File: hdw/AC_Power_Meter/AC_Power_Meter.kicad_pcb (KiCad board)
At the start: 2 copper layers, 100 x 100 mm, 272 parts, among them J1001 USB_B_Mini, J1701 Ext_SW_Toggle, J201 HT_IN, J202 NEUT_IN, J203 EARTH_IN, J401 HT_OUT, J402 NEUT_OUT, J403 EARTH_OUT, J501 AUX_IN, J801 Prog, Q1501 BT139-600, Q1701 2N7002, Q501 DMP3099L-7, SW1702 MRESET, SW1703 SW_Toggle, U1001 LT6700-1-S6, U1002 FT234XD, U1003 74LVC1G06, U1004 TPD3S014DBVR, U1101 ISO7321C, U1201 SSD1306, U1401 LTV-356T, U1402 74LVC1G17, U1501 74LVC1G32, U1502 FOD4218, U1601 74LVC1G06, U1602 74LVC1G06, U1603 74LVC1G06, U1604 74LVC1G06, U1605 74LVC1G06, U1606 74LVC1G06, U1607 74LVC1G06, U1701 TLC555CPS, U1702 TLC555CPS, U301 ACS722LLCTR-20AB, U501 LT6700-1-S6, U502 74LVC1G17, U601 74LVC1G17, U602 LT3973-DD, U701 PIC18LF67K40-I/PT, U801 TL331, U802 74LVC1G86, U901 LTC6240IS5, U902 LTC6240IS5, U903 LTC6240IS5, U904 LTC6240IS5, X701 ASV-16.000MHz

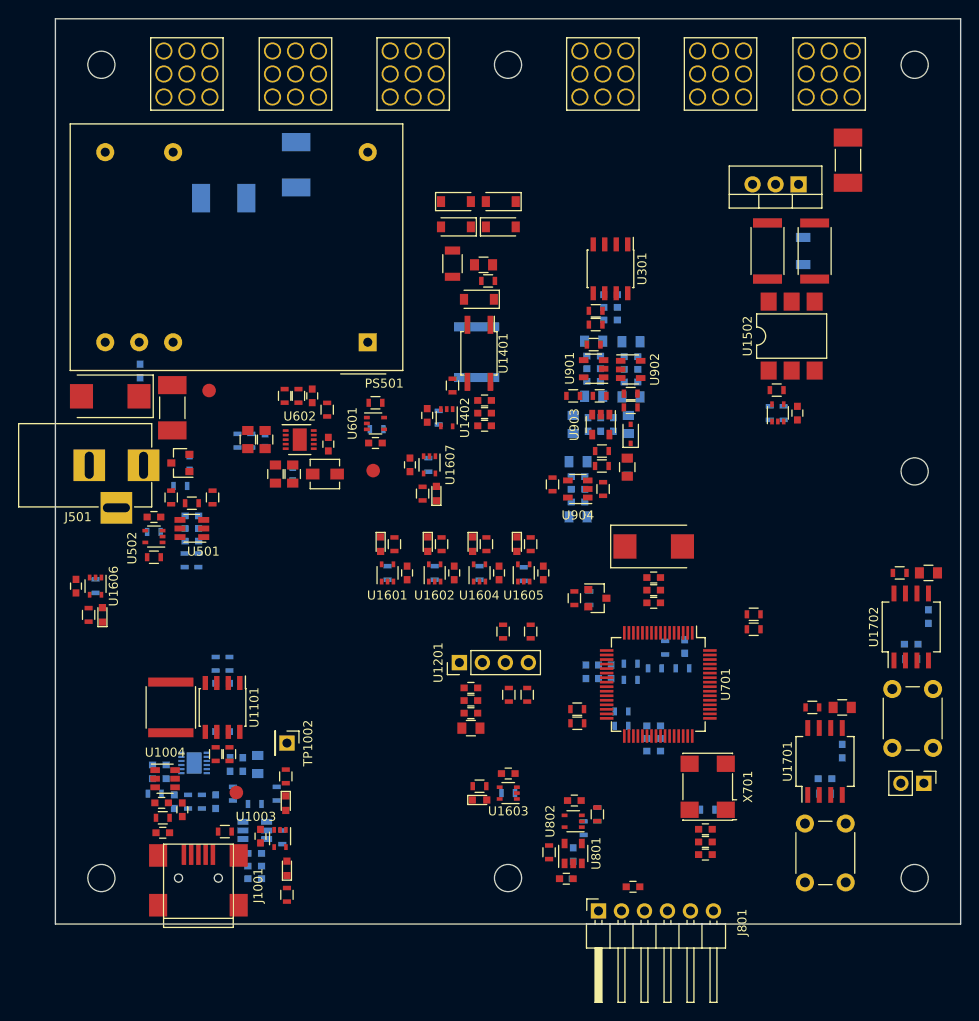
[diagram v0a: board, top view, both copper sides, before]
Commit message: Routed much more of the board, design rule fixes
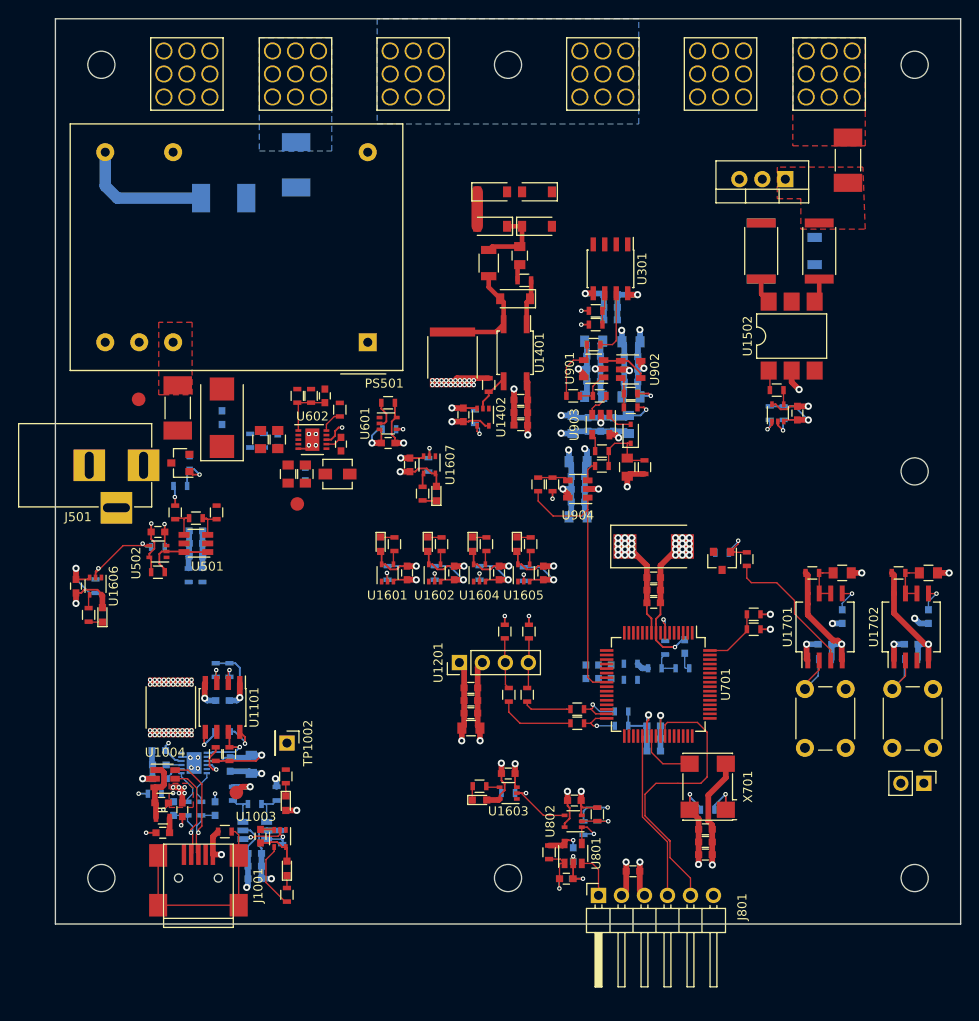
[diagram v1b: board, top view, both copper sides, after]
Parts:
- C1402, R907: moved to F.Cu
- moved R1706 19.5 mm to (148.0, 110.9)
- moved R1705 15.5 mm to (145.3, 110.2), turned to 180 degrees
- moved C1701 14.9 mm to (158.6, 117.2)
- moved C1705 14.9 mm to (158.6, 112.4)
- moved R1703 14.9 mm to (155.3, 112.4)
- moved U1701 14.9 mm to (156.7, 118.4)
- moved R1701 14.9 mm to (156.7, 121.9)
- moved SW1702 14.9 mm to (158.9, 125.2)
- moved C1703 14.9 mm to (156.7, 120.3)
- moved Q1701 14.4 mm to (145.3, 111.1), turned to 270 degrees
- moved C505 12.6 mm to (90.0, 95.2), turned to 90 degrees
- moved C504 10.4 mm to (90.0, 95.2)
- moved C1006 9.41 mm to (83.1, 132.0), turned to 180 degrees
- moved TP601 9.16 mm to (98.4, 104.8)
- moved TP501 7.84 mm to (80.8, 93.2)
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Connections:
- R1101 pad 2: GND -> +3V3
- R1102 pad 2: GND -> +3V3
- R1103 pad 2: GND_USB -> +5V_USB
- R1104 pad 2: GND_USB -> +5V_USB
- U1004 pad 5: /USB UART Bridge/CONN_USB+ -> /USB UART Bridge/CONN_USB-
- U1004 pad 6: /USB UART Bridge/CONN_USB- -> /USB UART Bridge/CONN_USB+
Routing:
- net +3V3: track 0.00 -> 214.7 mm, vias 0 -> 48
- net GND: track 0.00 -> 194.7 mm, vias 0 -> 98
- net +5V_USB: track 0.00 -> 40.4 mm, vias 0 -> 13
- net GND_USB: track 0.00 -> 33.1 mm, vias 0 -> 34
- net ICSPCLK: track 0.00 -> 32.4 mm
- net ISNS_ADC: track 0.00 -> 29.7 mm
- net Net-(J1001-Pad6): track 0.00 -> 23.1 mm
- net ICSPDAT: track 0.00 -> 18.8 mm
- net Net-(R1706-Pad2): track 0.00 -> 15.9 mm
- net /USB UART Bridge/CONN_USB+: track 0.00 -> 15.5 mm, vias 0 -> 1
- net Net-(F501-Pad1): track 0.00 -> 14.9 mm
- net /USB UART Bridge/CONN_USB-: track 0.00 -> 14.3 mm, vias 0 -> 1
- net POS12_PGOOD: track 0.00 -> 12.1 mm, vias 0 -> 2
- net GNDPWR: track 0.00 -> 12.0 mm
- net ~MCLR: track 0.00 -> 8.97 mm, vias 0 -> 1
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- added copper zone on PWR, net +3V3
- added copper zone on F.Cu, net +5V_USB
- added copper zone on PWR, net +5V_USB
- added copper zone on B.Cu, net Earth_Protective
- added copper zone on GND, net GND
- added copper zone on GND, net GND_USB
- added copper zone on B.Cu, net Net-(F201-Pad2)
- added copper zone on F.Cu, net Net-(F401-Pad1)
- added copper zone on F.Cu, net Net-(F502-Pad2)
- added copper zone on F.Cu, net TRIAC_HT_OUT
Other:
- copper layers 2 -> 4
- net class Default: trace_width 0.1016 -> 0.2032; via_dia 0.8 -> 0.5; via_drill 0.4 -> 0.25
- net class Power_HV_Tight added: clearance 0.127, trace_width 1.27, via_dia 0.8, via_drill 0.4
- net class Signal: trace_width 0.1016 -> 0.1524
- board text added: "* Add MU Logo * Label all LEDs * Label all connectors * Add layer copper labels * Add ESD warning * Add high voltage warning"

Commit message: MOAR ROUTING
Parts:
- C301, C302, C303: moved to F.Cu
- R301, R302, U301: moved to B.Cu
- moved D1404 12.3 mm to (117.1, 82.2), turned to 90 degrees
- moved D1401 12.1 mm to (113.2, 77.3), turned to 90 degrees
- moved D1403 10.6 mm to (113.2, 82.2), turned to 270 degrees
- moved D1402 10.4 mm to (117.1, 77.3), turned to 270 degrees
- moved R606 4.23 mm to (95.6, 94.4), turned to 90 degrees
- moved R301 3.88 mm to (135.1, 83.9), turned to 180 degrees
- moved R302 3.88 mm to (135.1, 82.4), turned to 180 degrees
- moved R605 3.48 mm to (94.1, 94.4), turned to 270 degrees
- moved C1403 1.59 mm to (123.7, 94.7)
- moved U1402 1.59 mm to (119.5, 96.6)
- moved C1402 1.59 mm to (116.1, 90.0)
- moved R1401 1.59 mm to (120.1, 79.6)
- moved R1402 1.59 mm to (124.1, 81.5)
- moved R1404 1.59 mm to (118.6, 96.6)
- moved C1404 1.59 mm to (123.7, 96.1)
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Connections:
- U301 pad 1: ISNS_HT_OUT -> HT
- U301 pad 2: ISNS_HT_OUT -> HT
- U301 pad 3: HT -> ISNS_HT_OUT
- U301 pad 4: HT -> ISNS_HT_OUT
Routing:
- net NEUT: track 3.81 -> 44.9 mm
- net ISNS_HT_OUT: track 0.00 -> 30.0 mm
- net HT: track 0.00 -> 26.8 mm, vias 0 -> 1
- net Net-(Q1501-Pad3): track 2.70 -> 28.7 mm
- net TRIAC_HT_OUT: track 0.00 -> 24.7 mm
- net GND: track 194.7 -> 214.8 mm, vias 98 -> 100
- net Net-(C1401-Pad2): track 7.58 -> 18.1 mm, vias 0 -> 2
- net Net-(C605-Pad2): track 0.00 -> 8.76 mm
- net Net-(C1502-Pad1): track 0.00 -> 6.57 mm
- net GNDPWR: track 12.0 -> 16.9 mm
- net Net-(C1014-Pad1): track 1.65 -> 4.72 mm
- net +3V3: track 214.7 -> 216.3 mm
- net ISNS_OUT: track 7.16 -> 7.07 mm, vias 0 -> 1
- added copper zone on F.Cu, net +3V3
- added copper zone on B.Cu, net HT
- added copper zone on B.Cu, net ISNS_HT_OUT
- added copper zone on F.Cu, net NEUT
- added copper zone on F.Cu, net Net-(C605-Pad2)
- added copper zone on F.Cu, net Net-(J501-Pad1)

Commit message: Finished routing, adding bells and whistles
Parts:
- added G***: MU_Logo, Custom Footprints Library:MU_Logo, F.Cu at (100.1, 119.4)
- moved C607 6.52 mm to (104.7, 97.9), turned to 270 degrees
- moved TP601 3.66 mm to (97.1, 108.2)
- moved R1706 2.23 mm to (150.2, 111.0)
- moved Q1701 2.23 mm to (147.5, 111.2)
- moved R1705 2.23 mm to (147.5, 110.3)
- moved C604 1.52 mm to (95.9, 97.8)
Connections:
- R1501 pad 1: SSR_Force -> SSR_Dim
- R1502 pad 1: SSR_Dim -> SSR_Force
- U1501 pad 1: SSR_Force -> SSR_Dim
- U1501 pad 2: SSR_Dim -> SSR_Force
- U701 pad 1: POS12_PGOOD -> (no net)
- U701 pad 2: POS12_ADC -> (no net)
- U701 pad 27: (no net) -> Zero_Cross_Detect
- U701 pad 28: (no net) -> POS12_ADC
- U701 pad 33: (no net) -> POS3P3_PGOOD
- U701 pad 34: (no net) -> POS12_PGOOD
- U701 pad 47: SW_Toggle -> (no net)
- U701 pad 48: Zero_Cross_Detect -> SW_Toggle
- U701 pad 63: POS3P3_PGOOD -> (no net)
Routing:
- net +12V: track 7.92 -> 121.4 mm, vias 1 -> 4
- net POS3P3_PGOOD: track 3.52 -> 85.6 mm
- net POS12_PGOOD: track 12.1 -> 87.2 mm
- net Zero_Cross_Detect: track 2.30 -> 69.6 mm
- net POS12_ADC: track 0.00 -> 66.1 mm, vias 0 -> 1
- net ~MCLR: track 8.97 -> 73.4 mm, vias 1 -> 2
- net USB_UART_TX: track 2.23 -> 50.3 mm, vias 1 -> 3
- net USB_UART_RX: track 2.23 -> 48.8 mm, vias 1 -> 3
- net SW_Toggle: track 0.00 -> 31.3 mm, vias 0 -> 2
- net ~Active: track 1.75 -> 32.9 mm, vias 1 -> 2
- net SSR_Force: track 2.19 -> 30.1 mm
- net +3V3: track 216.3 -> 243.8 mm, vias 48 -> 148
- net SSR_Dim: track 2.40 -> 29.8 mm
- net Comm_Error: track 1.57 -> 27.4 mm, vias 1 -> 2
- net Heartbeat: track 1.57 -> 22.3 mm, vias 1 -> 2
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- added copper zone on F.Cu, net +12V

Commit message: Added a few more finishing touches, moved some components
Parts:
- removed the G*** at (100.1, 119.4)
- added G***: MU_Logo_Silk, Custom Footprints Library:MU_Logo_Silk, F.Cu at (105.7, 128.7)
- added G***: Microchip_Logo, Custom Footprints Library:Microchip_Logo, F.Cu at (138.2, 124.7)
- added REF***: ESD-Logo_6.6x6mm_SilkScreen, Symbols:ESD-Logo_6.6x6mm_SilkScreen, B.Cu at (140.6, 82.7)
- added REF***: ESD-Logo_6.6x6mm_SilkScreen, Symbols:ESD-Logo_6.6x6mm_SilkScreen, F.Cu at (140.4, 94.5)
- added REF***: ESD-Logo_6.6x6mm_SilkScreen, Symbols:ESD-Logo_6.6x6mm_SilkScreen, F.Cu at (136.6, 134.9)
- added TP502: TP, Pin_Headers:Pin_Header_Angled_1x01_Pitch2.54mm, F.Cu at (103.1, 149.3)
- TP1002: footprint Pin_Headers:Pin_Header_Straight_1x01_Pitch2.54mm -> Pin_Headers:Pin_Header_Angled_1x01_Pitch2.54mm
- moved TP1002 22.8 mm to (74.4, 130.4)
- moved R1614 5.32 mm to (113.8, 98.6), turned to 270 degrees
- moved D1607 5.29 mm to (112.3, 98.6), turned to 270 degrees
- moved C1607 4.56 mm to (115.2, 101.7), turned to 270 degrees
- moved J1701 4.00 mm to (167.6, 139.6)
- moved R1613 1.31 mm to (113.2, 101.7), turned to 90 degrees
- moved U1607 1.27 mm to (113.0, 101.7), turned to 90 degrees
- moved C1605 1.27 mm to (126.8, 112.4)
- moved D1605 1.27 mm to (123.9, 109.2)
- moved R1609 1.27 mm to (124.7, 112.5)
- moved R1611 1.27 mm to (125.4, 109.2)
- moved U1605 1.27 mm to (124.7, 112.4)
- moved C1402 0.89 mm to (116.1, 89.2)
- moved D1601 0.64 mm to (106.9, 109.2)
- moved D1604 0.64 mm to (118.4, 109.2)
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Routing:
- net HT: track 26.8 -> 6.03 mm
- net POS3P3_PGOOD: track 85.6 -> 76.2 mm, vias 2 -> 4
- net Net-(J1701-Pad2): track 18.4 -> 22.4 mm
- net GND_USB: track 35.2 -> 37.0 mm, vias 35 -> 34
- net ADC_Error: track 17.1 -> 15.5 mm
- net Heartbeat: track 22.3 -> 21.3 mm
- net GND: track 229.0 -> 228.1 mm
- net ~Active: track 32.9 -> 33.4 mm
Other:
- board text added: "* Label all connectors * Add layer copper labels * Add ESD warning * Add high voltage warning * Add class label * Add project name * Add soldermask MU logo"
- board text added: "+12V"
- board text added: "+12V PGOOD"
- board text added: "+3.3V"
- board text added: "+3.3V PGOOD"
- board text added: "+5V USB"
- board text added: "ADC Error"
- board text added: "Comm Error"
- board text added: "GND"
- board text added: "GND IN"
- board text added: "GND OUT"
- board text added: "GND USB"
- board text added: "HRTBT"
- board text added: "HT IN"
- board text added: "HT OUT"
- board text added: "Manual Reset"
- board text added: "NEUT IN"
- board text added: "NEUT OUT"
- board text added: "Output Toggle"
- board text added: "PROG"
- board text added: "Reset"
- board text removed: "* Add MU Logo * Label all LEDs * Label all connectors * Add layer copper labels * Add ESD warning * Add high voltage warning"

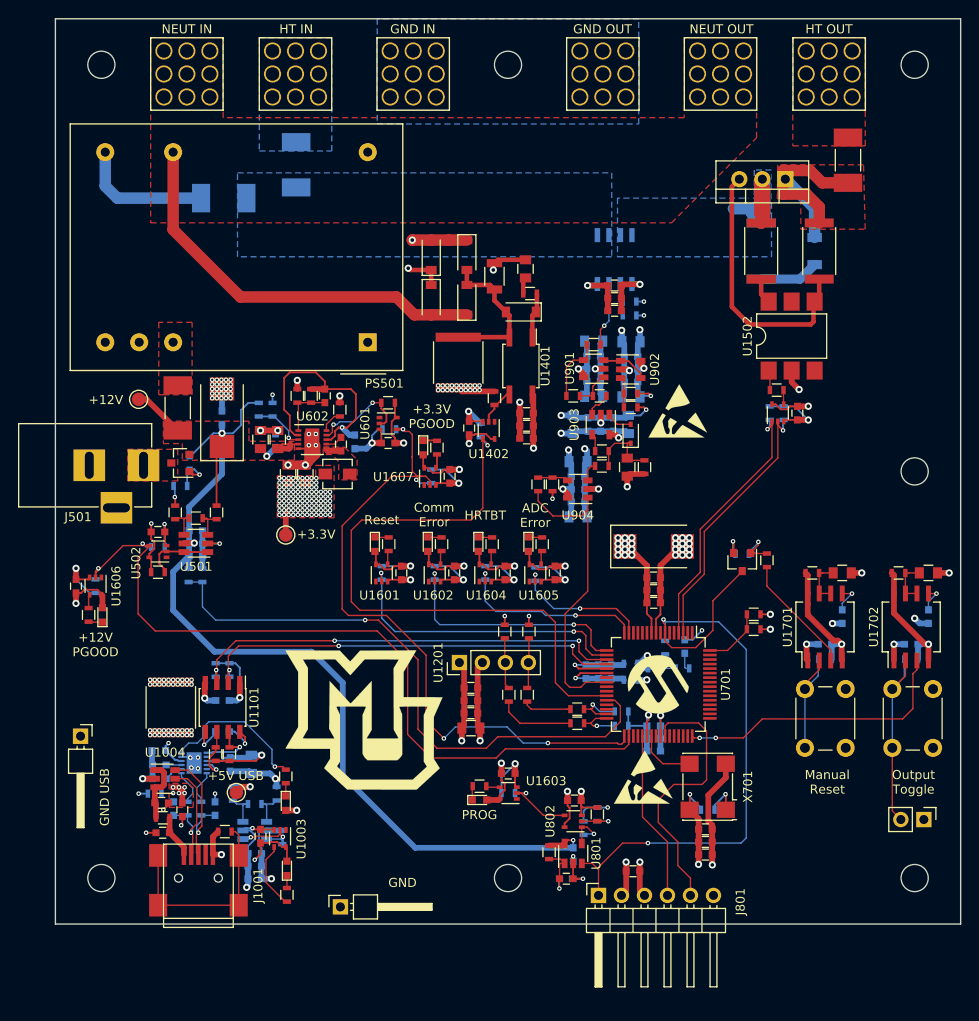
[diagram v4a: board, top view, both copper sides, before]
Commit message: A few routing adjustments and more graphics added to PCB
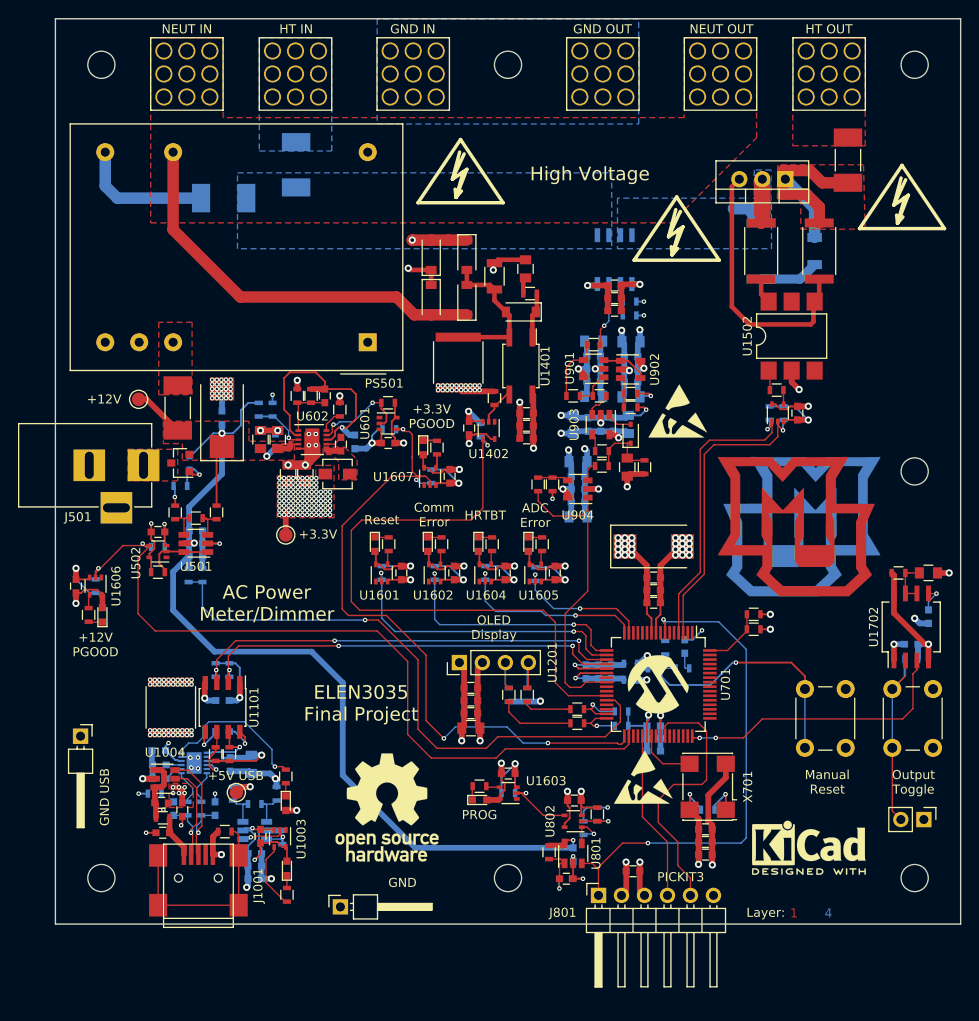
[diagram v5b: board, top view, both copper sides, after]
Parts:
- removed C1701: 10nF, Capacitors_SMD:C_0603
- removed C1703: 0.1uF, Capacitors_SMD:C_0603
- removed C1705: 1uF, Capacitors_SMD:C_0805
- removed the G*** at (105.7, 128.7)
- removed Q1701: 2N7002, TO_SOT_Packages_SMD:SOT-23
- removed R1701, R1705: 10k, Resistors_SMD:R_0603
- removed R1703: 100k, Resistors_SMD:R_0603
- removed R1706: 220, Resistors_SMD:R_0603
- removed U1701: TLC555CPS, Housings_SOIC:SO-8_5.3x6.2mm_Pitch1.27mm
- added G***: MU_Logo_Copper, Custom Footprints Library:MU_Logo_Copper, F.Cu at (153.4, 107.3)
- added G***: MU_Logo_Mask, Custom Footprints Library:MU_Logo_Mask, F.Cu at (153.4, 107.3)
- added G***: MU_Logo_Mask, Custom Footprints Library:MU_Logo_Mask, B.Cu at (154.2, 107.3)
- added G***: MU_Logo_Copper, Custom Footprints Library:MU_Logo_Copper, B.Cu at (154.2, 107.3)
- added REF**: Symbol_HighVoltage_Type2_Silkscreen_VerySmall, Custom Footprints Library:Symbol_HighVoltage_Type2_Silkscreen_VerySmall, B.Cu at (81.0, 72.5)
- added REF**: Symbol_HighVoltage_Type2_Silkscreen_VerySmall, Custom Footprints Library:Symbol_HighVoltage_Type2_Silkscreen_VerySmall, B.Cu at (165.2, 68.4)
- added REF**: Symbol_HighVoltage_Type2_Silkscreen_VerySmall, Custom Footprints Library:Symbol_HighVoltage_Type2_Silkscreen_VerySmall, B.Cu at (116.4, 71.2)
- added REF**: Symbol_HighVoltage_Type2_Silkscreen_VerySmall, Custom Footprints Library:Symbol_HighVoltage_Type2_Silkscreen_VerySmall, F.Cu at (140.3, 75.1)
- added REF**: Symbol_HighVoltage_Type2_Silkscreen_VerySmall, Custom Footprints Library:Symbol_HighVoltage_Type2_Silkscreen_VerySmall, F.Cu at (165.2, 71.6)
- added REF**: Symbol_HighVoltage_Type2_Silkscreen_VerySmall, Custom Footprints Library:Symbol_HighVoltage_Type2_Silkscreen_VerySmall, F.Cu at (116.4, 68.7)
- added REF***: OSHW-Logo_11.4x12mm_SilkScreen, Symbols:OSHW-Logo_11.4x12mm_SilkScreen, F.Cu at (108.3, 138.3)
- added REF***: KiCad-Logo2_6mm_SilkScreen, Symbols:KiCad-Logo2_6mm_SilkScreen, F.Cu at (154.9, 142.7)
- R1203, R1204: moved to B.Cu
- moved REF*** 13.4 mm to (127.3, 81.1)
- moved R1203 7.00 mm to (121.7, 125.9), turned to 90 degrees
- moved R1204 6.99 mm to (123.8, 125.9), turned to 90 degrees
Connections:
- R805 pad 2: Net-(R805-Pad2) -> ~MRST
- R806 pad 2: Net-(R805-Pad2) -> ~MRST
- R807 pad 2: Net-(R805-Pad2) -> ~MRST
- SW1702 pad 2: Net-(R1701-Pad2) -> ~MRST
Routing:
- net ~MRST: track 0.00 -> 30.0 mm, vias 0 -> 1
- net ~MCLR: track 73.4 -> 58.2 mm
- net Net-(R1701-Pad2): track 14.2 -> 0.00 mm
- net Net-(R1706-Pad2): track 13.2 -> 0.00 mm
- net +3V3: track 243.5 -> 230.7 mm, vias 148 -> 146
- net GND: track 228.1 -> 219.9 mm, vias 133 -> 129
- net Net-(Q1701-Pad1): track 5.13 -> 0.00 mm, vias 1 -> 0
- net Net-(C1705-Pad1): track 5.10 -> 0.00 mm
- net SSR_Force: track 30.1 -> 33.7 mm
- net SSR_Dim: track 29.8 -> 33.4 mm
- net Net-(C1701-Pad1): track 3.32 -> 0.00 mm, vias 1 -> 0
- net Net-(R805-Pad2): track 3.25 -> 0.00 mm
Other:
- board text added: "1"
- board text added: "2"
- board text added: "3"
- board text added: "4"
- board text added: "AC Power Meter/Dimmer"
- board text added: "ELEN3035 Final Project"
- board text added: "High Voltage"
- board text added: "Layer:"
- board text added: "OLED Display"
- board text added: "PICKIT3"
- board text removed: "* Label all connectors * Add layer copper labels * Add ESD warning * Add high voltage warning * Add class label * Add project name * Add soldermask MU logo"
